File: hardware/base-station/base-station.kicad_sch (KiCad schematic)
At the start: 0 parts

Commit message: Added schematic for base station
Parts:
- added C1, C2: 4.7μF, Capacitor_SMD:C_0402_1005Metric, symbol Device:C
- added Conn1: Magnetic Connector, Custom_Footprints:Connector_Magnetic_4_Pin, symbol Custom_Symbols:Conn_01x04_Magnetic
- added D1: SMAJ5.0A, Diode_SMD:D_SMA, symbol Diode:SMAJ5.0A
- added D2: LTST-C235KGKRKT, LED_SMD:LED_LiteOn_LTST-C235KGKRKT, symbol LED:LTST-C235KGKRKT
- added J1: USB_C_Receptacle_USB2.0_16P, Connector_USB:USB_C_Receptacle_GCT_USB4105-xx-A_16P_TopMnt_Horizontal, symbol Connector:USB_C_Receptacle_USB2.0_16P
- added R1, R2: 10kΩ, symbol Device:R_US
- added U1: MCP73831-2-OT, Package_TO_SOT_SMD:SOT-23-5, symbol Battery_Management:MCP73831-2-OT
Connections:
- new net: R2.1, U1.1 (STAT)
- new net: R1.2, U1.5 (PROG)
- new net: Conn1.2 (DATA+), J1.A6 (D+), J1.B6 (D+)
- new net: Conn1.3 (DATA-), J1.A7 (D-), J1.B7 (D-)
- new net: D2.2 (A2), D2.4 (K1), R2.2
- new net GND: C1.2, C2.2, Conn1.4 (GND), D1.2 (A2), J1.A1 (GND), J1.A12 (GND), J1.B1 (GND), J1.B12 (GND), J1.S1 (SHIELD), R1.1, U1.2 (V_{SS})
- new net V_{BAT}: C1.1, Conn1.1 (VIN), U1.3 (V_{BAT})
- new net V_{EXT}: C2.1, D1.1 (A1), D2.1 (K2), D2.3 (A1), J1.A4 (VBUS), J1.A9 (VBUS), J1.B4 (VBUS), J1.B9 (VBUS), U1.4 (V_{DD})
- no-connect marks 0 -> 4

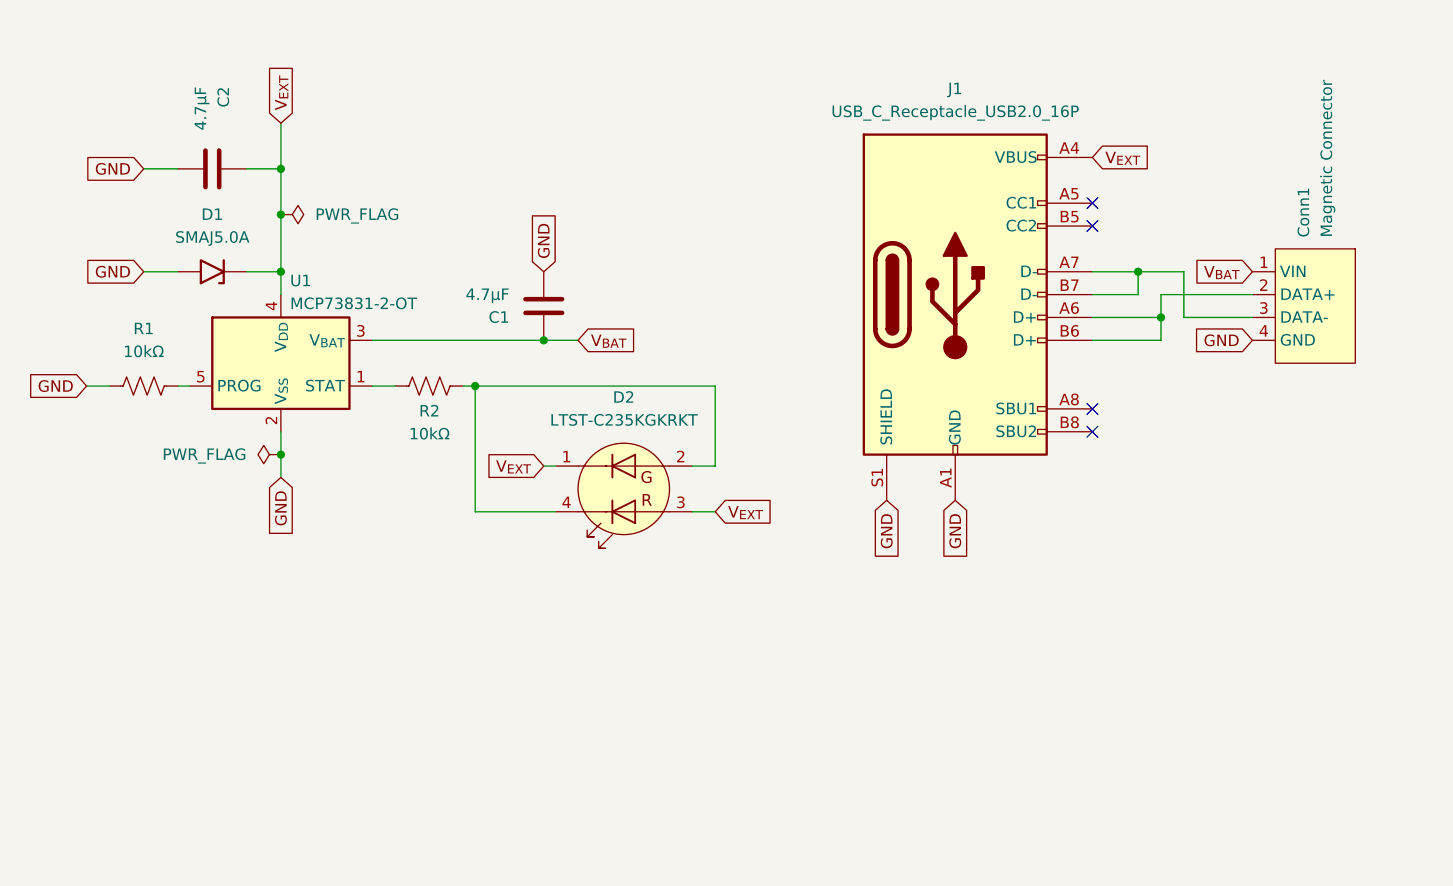
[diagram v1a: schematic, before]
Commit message: Replaced MCP73831T with TPB4056A
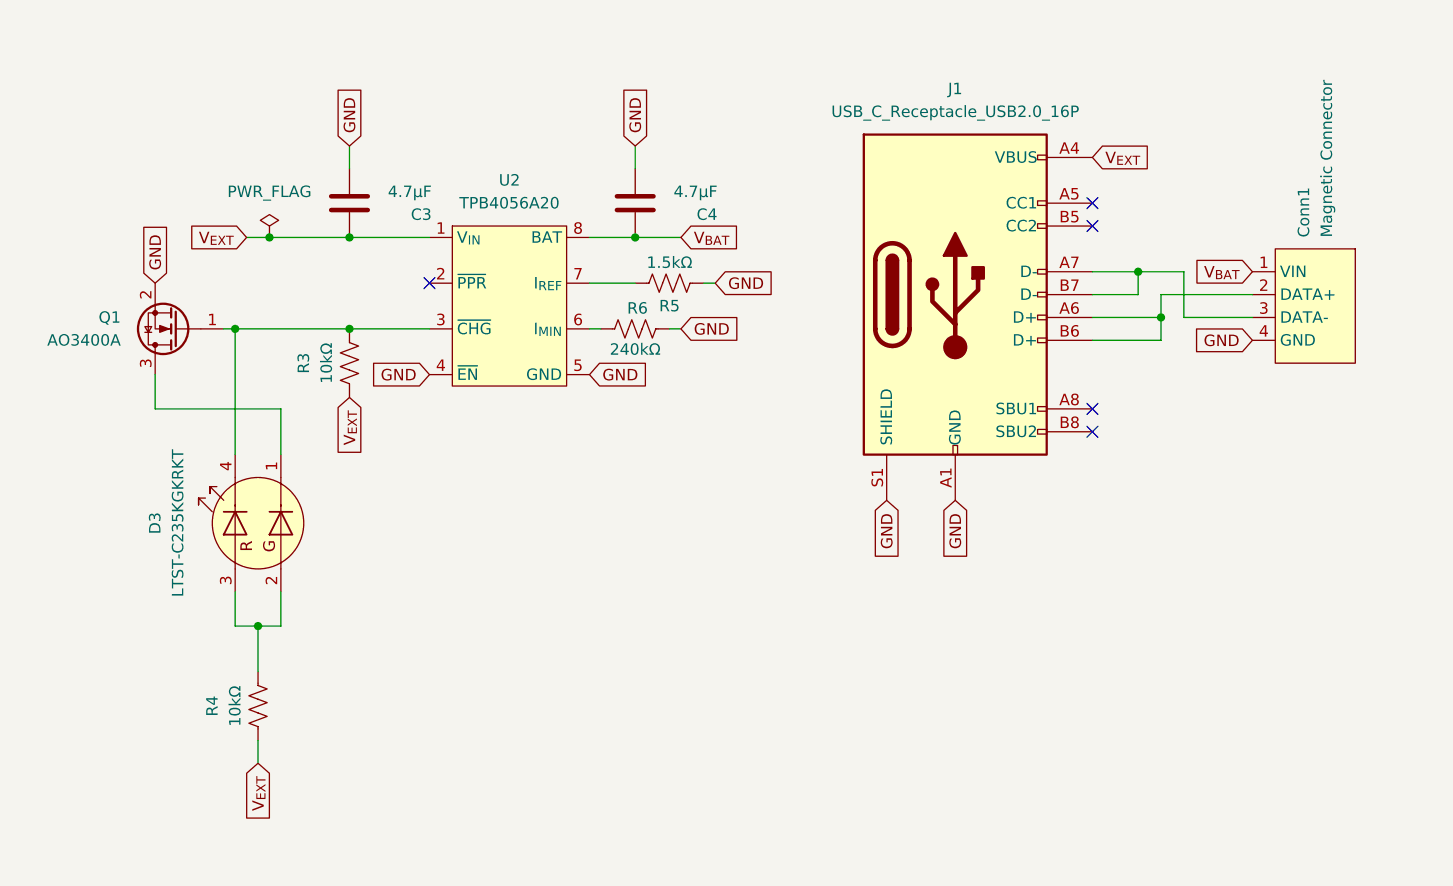
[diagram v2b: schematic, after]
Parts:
- removed C1, C2: 4.7μF, Capacitor_SMD:C_0402_1005Metric, symbol Device:C
- removed D1: SMAJ5.0A, Diode_SMD:D_SMA, symbol Diode:SMAJ5.0A
- removed D2: LTST-C235KGKRKT, LED_SMD:LED_LiteOn_LTST-C235KGKRKT, symbol LED:LTST-C235KGKRKT
- removed R1, R2: 10kΩ, symbol Device:R_US
- removed U1: MCP73831-2-OT, Package_TO_SOT_SMD:SOT-23-5, symbol Battery_Management:MCP73831-2-OT
- added C3, C4: 4.7μF, Capacitor_SMD:C_0402_1005Metric, symbol Device:C
- added D3: LTST-C235KGKRKT, LED_SMD:LED_LiteOn_LTST-C235KGKRKT, symbol LED:LTST-C235KGKRKT
- added Q1: AO3400A, Package_TO_SOT_SMD:SOT-23, symbol Transistor_FET:AO3400A
- added R3, R4: 10kΩ, symbol Device:R_US
- added R5: 1.5kΩ, symbol Device:R_US
- added R6: 240kΩ, symbol Device:R_US
- added U2: TPB4056A20, Package_SO:SOP-8-1EP_4.57x4.57mm_P1.27mm_EP4.57x4.45mm_ThermalVias, symbol Custom_Symbols:TPB4056A20
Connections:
- net GND: now also C3.2, C4.2, Q1.2 (S), R5.1, R6.1, U2.4 (~{EN}), U2.5 (GND)
- net V_{BAT}: now also C4.1, U2.8 (BAT)
- net V_{EXT}: now also C3.1, R3.1, R4.1, U2.1 (V_{IN})
- new net: D3.4 (K1), Q1.1 (G), R3.2, U2.3 (~{CHG})
- new net: R5.2, U2.7 (I_{REF})
- new net: R6.2, U2.6 (I_{MIN})
- new net: D3.1 (K2), Q1.3 (D)
- new net: D3.2 (A2), D3.3 (A1), R4.2
- no-connect marks 4 -> 5

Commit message: Fixed minor ERC issues on base station
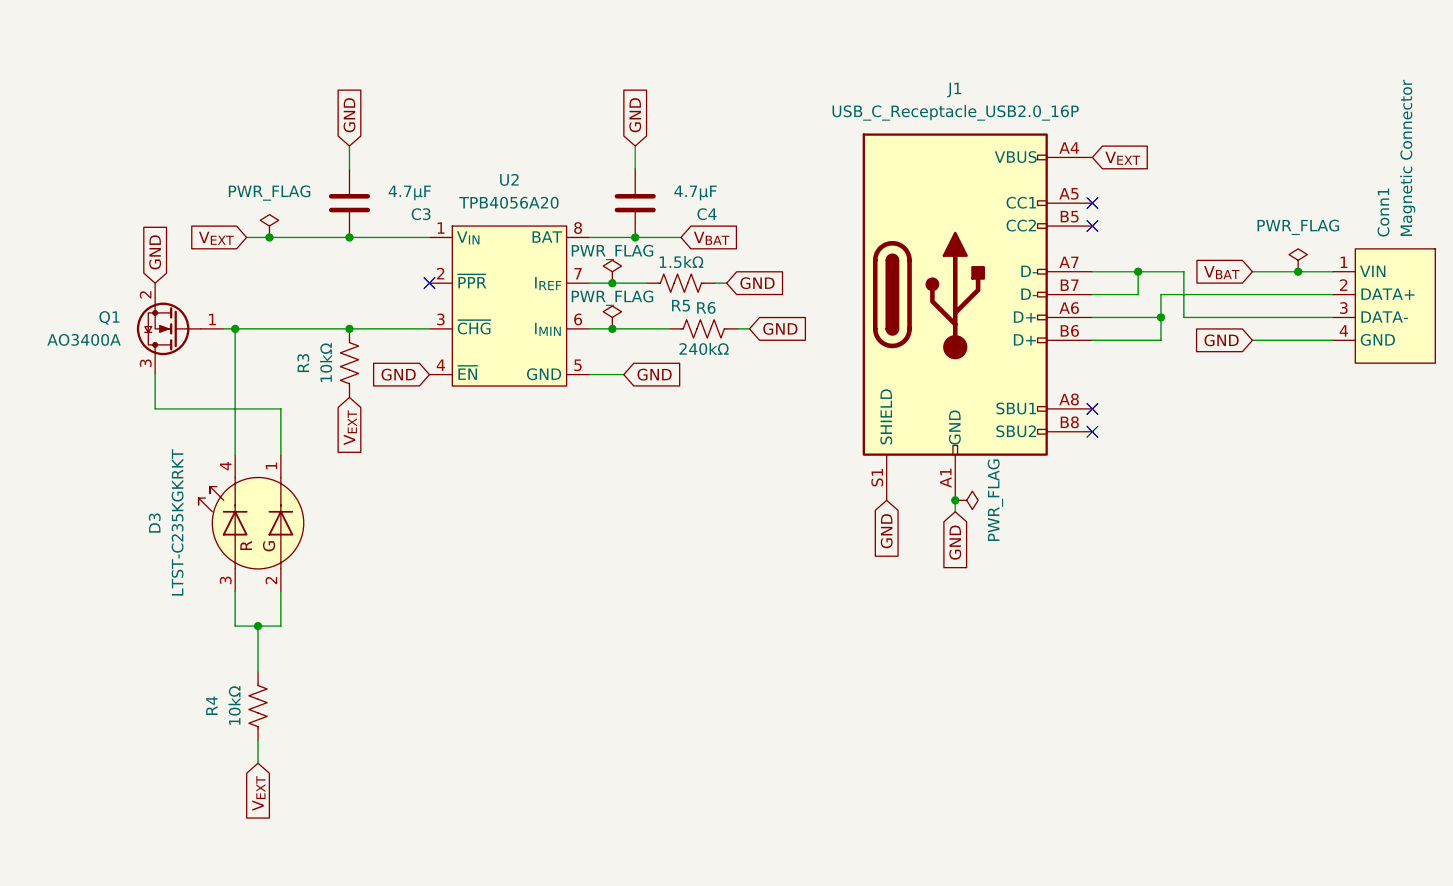
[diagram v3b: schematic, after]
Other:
- moved on the sheet: Conn1, R5, R6

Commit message: Added missing footprint assignments
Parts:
- R3, R4, R5, R6: footprint (none) -> Resistor_SMD:R_0805_2012Metric_Pad1.20x1.40mm_HandSolder
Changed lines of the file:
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@@
 			)
 		)
-		(property "Footprint" ""
+		(property "Footprint" "Resistor_SMD:R_0805_2012Metric_Pad1.20x1.40mm_HandSolder"
 			(at 49.784 46.736 90)
 			(effects
@@
 			)
 		)
-		(property "Footprint" ""
+		(property "Footprint" "Resistor_SMD:R_0805_2012Metric_Pad1.20x1.40mm_HandSolder"
 			(at 87.376 39.116 90)
 			(effects
@@
 			)
 		)
-		(property "Footprint" ""
+		(property "Footprint" "Resistor_SMD:R_0805_2012Metric_Pad1.20x1.40mm_HandSolder"
 			(at 89.916 44.196 90)
 			(effects
@@
 			)
 		)
-		(property "Footprint" ""
+		(property "Footprint" "Resistor_SMD:R_0805_2012Metric_Pad1.20x1.40mm_HandSolder"
 			(at 39.624 84.836 90)
 			(effects
